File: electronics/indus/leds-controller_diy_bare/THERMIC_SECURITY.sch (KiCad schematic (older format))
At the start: 8 parts

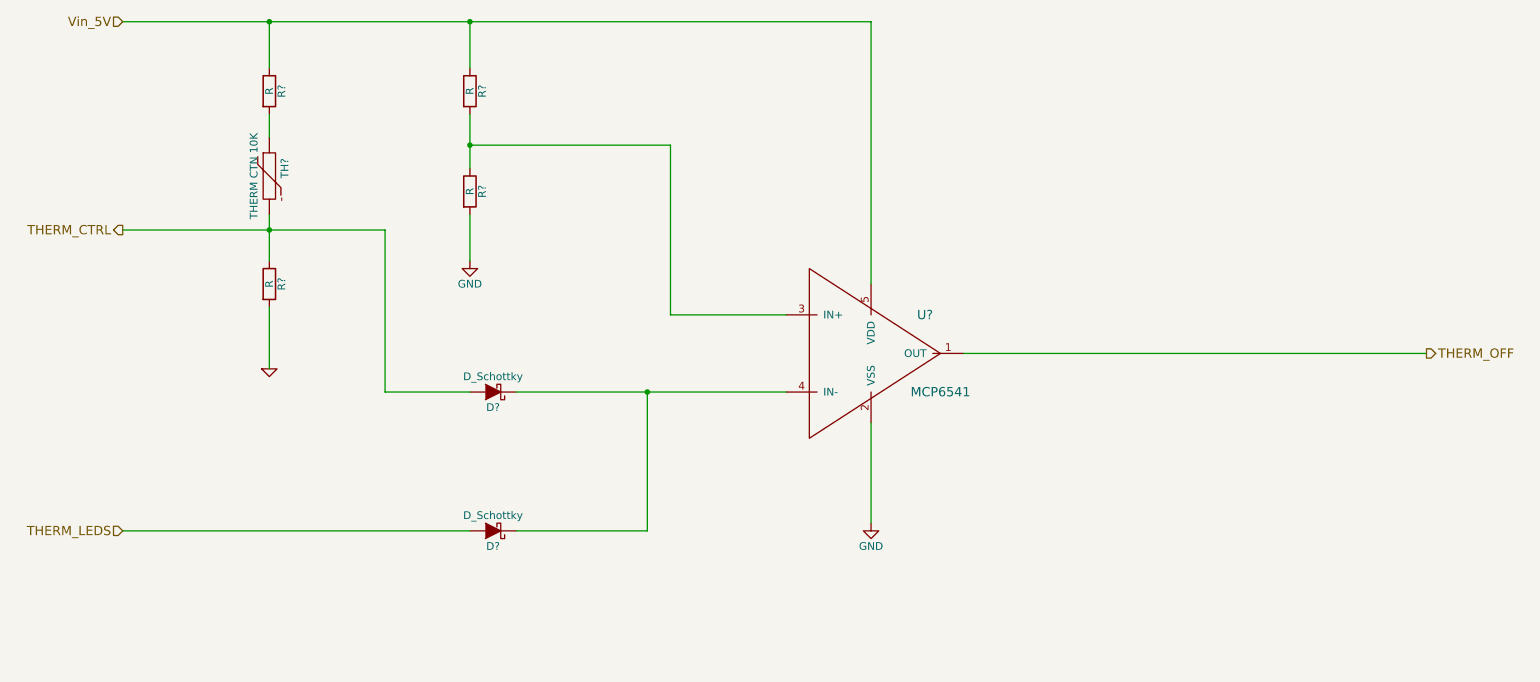
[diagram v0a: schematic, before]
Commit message: schema prctically ok missing refs
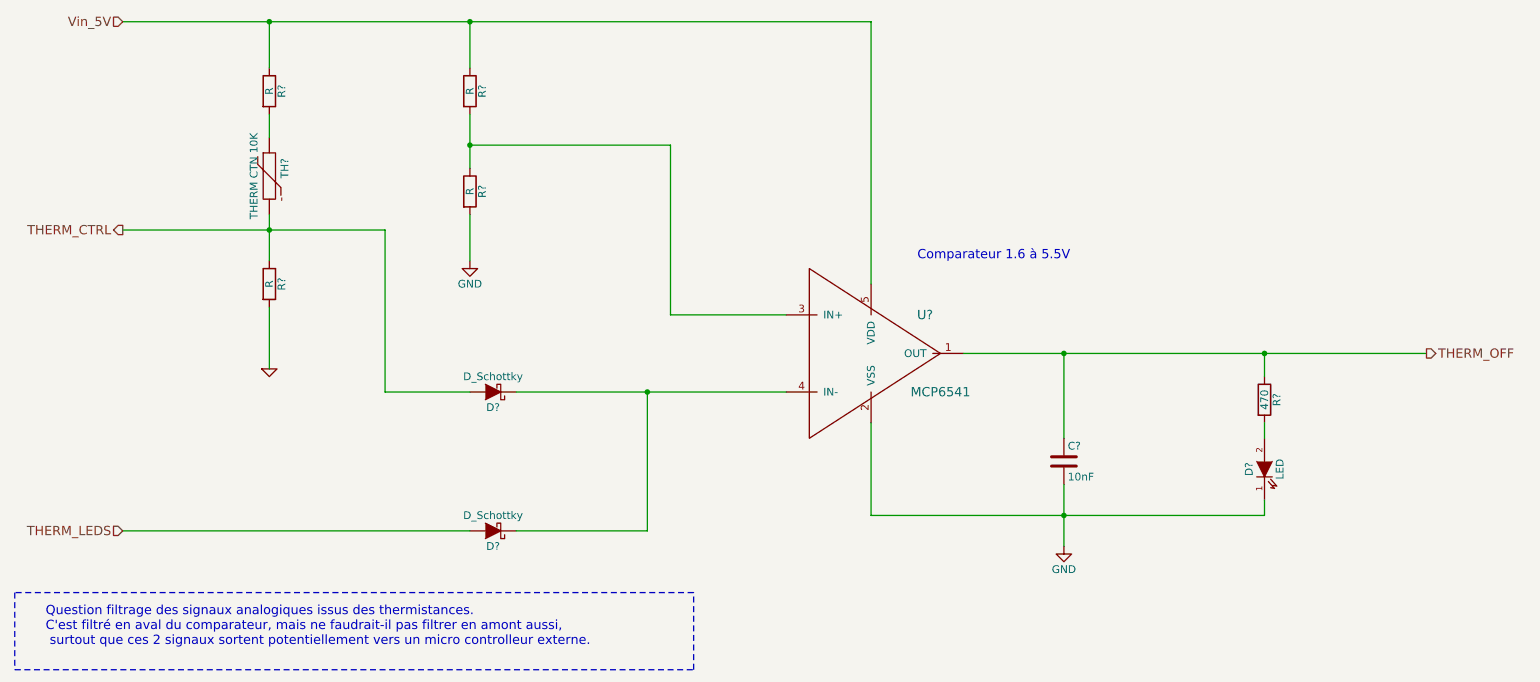
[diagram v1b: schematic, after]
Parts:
- added C?: 10nF, symbol C
- added D?: LED, symbol LED
- added R?: 470, symbol R
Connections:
- net GND: now also C?.2, D?.1 (K)
- net THERM_OFF: now also C?.1, R?.1
- new net: D?.2 (A), R?.2
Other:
- note added: "Comparateur 1.6 à 5.5V"
- note added: "Question filtrage des signaux analogiques issus des thermistances. \nC'est filtré en aval du comparateur, mais ne faudrait-il pas filtrer en amont aussi,\n surtout que ces 2 signaux sortent potentiellement vers un micro controlleur externe."
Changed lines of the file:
@@
 	1450 4950 3700 4950
 Wire Wire Line
-	1450 1650 2400 1650
-Wire Wire Line
-	2400 1650 3700 1650
-Wire Wire Line
-	3700 1650 6300 1650
+	1450 1650 6300 1650
 Wire Wire Line
 	6300 1650 6300 3350
-$Comp
-L GND #PWR?
-U 1 1 57638CC5
-P 6300 4900
-F 0 "#PWR?" H 6300 4650 50  0001 C CNN
-F 1 "GND" H 6300 4750 50  0000 C CNN
-F 2 "" H 6300 4900 50  0000 C CNN
-F 3 "" H 6300 4900 50  0000 C CNN
-	1    6300 4900
-	1    0    0    -1
-$EndComp
 Wire Wire Line
-	6300 4250 6300 4900
+	6300 4250 6300 4850
 $Comp
 L R R?
@@
 	3700 3200 3700 2900
 Wire Wire Line
-	3700 2250 3700 2450
-Wire Wire Line
-	3700 2450 3700 2600
+	3700 2250 3700 2600
 Wire Wire Line
 	3700 1950 3700 1650
@@
 $EndComp
 Wire Wire Line
-	2400 2900 2400 3000
+	2400 2900 2400 3200
 Wire Wire Line
-	2400 3000 2400 3200
-Wire Wire Line
-	1450 3000 2400 3000
-Wire Wire Line
-	2400 3000 3150 3000
+	1450 3000 3150 3000
 Wire Wire Line
 	3150 4050 3700 4050
 Wire Wire Line
-	4000 4050 4850 4050
-Wire Wire Line
-	4850 4050 5750 4050
+	4000 4050 5750 4050
 Wire Wire Line
 	4000 4950 4850 4950
@@
 Text HLabel 1450 3000 0    60   Output ~ 0
 THERM_CTRL
+$Comp
+L GND #PWR?
+U 1 1 5763C8DD
+P 7550 5050
+F 0 "#PWR?" H 7550 4800 50  0001 C CNN
+F 1 "GND" H 7550 4900 50  0000 C CNN
+F 2 "" H 7550 5050 50  0000 C CNN
+F 3 "" H 7550 5050 50  0000 C CNN
+	1    7550 5050
+	1    0    0    -1
+$EndComp
+$Comp
+L C C?
+U 1 1 5763C901
+P 7550 4500
+F 0 "C?" H 7575 4600 50  0000 L CNN
+F 1 "10nF" H 7575 4400 50  0000 L CNN
+F 2 "" H 7588 4350 50  0000 C CNN
+F 3 "" H 7550 4500 50  0000 C CNN
+	1    7550 4500
+	1    0    0    -1
+$EndComp
+Wire Wire Line
+	7550 4350 7550 3800
+Connection ~ 7550 3800
+Wire Wire Line
+	7550 4650 7550 5050
+$Comp
+L LED D?
+U 1 1 576465EC
+P 8850 4550
+F 0 "D?" H 8850 4650 50  0000 C CNN
+F 1 "LED" H 8850 4450 50  0000 C CNN
+F 2 "" H 8850 4550 50  0000 C CNN
+F 3 "" H 8850 4550 50  0000 C CNN
+	1    8850 4550
+	0    -1   -1   0
+$EndComp
+Connection ~ 8850 3800
+Wire Wire Line
+	6300 4850 8850 4850
+Connection ~ 7550 4850
+$Comp
+L R R?
+U 1 1 5764C339
+P 8850 4100
+F 0 "R?" V 8930 4100 50  0000 C CNN
+F 1 "470" V 8850 4100 50  0000 C CNN
+F 2 "" V 8780 4100 50  0000 C CNN
+F 3 "" H 8850 4100 50  0000 C CNN
+	1    8850 4100
+	1    0    0    -1
+$EndComp
+Wire Wire Line
+	8850 3800 8850 3950
+Wire Wire Line
+	8850 4250 8850 4350
+Wire Wire Line
+	8850 4850 8850 4750
+Text Notes 950  5700 0    60   ~ 0
+Question filtrage des signaux analogiques issus des thermistances. \nC'est filtré en aval du comparateur, mais ne faudrait-il pas filtrer en amont aussi,\n surtout que ces 2 signaux sortent potentiellement vers un micro controlleur externe.
+Wire Notes Line
+	750  5850 5150 5850
+Wire Notes Line
+	5150 5850 5150 5350
+Wire Notes Line
+	5150 5350 750  5350
+Wire Notes Line
+	750  5350 750  5850
+Text Notes 6600 3200 0    60   ~ 0
+Comparateur 1.6 à 5.5V
 $EndSCHEMATC

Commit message: schema prctically ok missing refs
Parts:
- gave numbers to parts that had none: 11
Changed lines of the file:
@@
 THERM_OFF
 $Comp
-L THERMISTOR TH?
+L THERMISTOR TH1
 U 1 1 57630E89
 P 2400 2650
-F 0 "TH?" V 2500 2700 50  0000 C CNN
+F 0 "TH1" V 2500 2700 50  0000 C CNN
 F 1 "THERM CTN 10K" V 2300 2650 50  0000 C CNN
 F 2 "" H 2400 2650 60  0000 C CNN
@@
 $EndComp
 $Comp
-L GND-RESCUE-leds-controller #PWR?
+L GND-RESCUE-leds-controller #PWR19
 U 1 1 57630E97
 P 2400 3900
-F 0 "#PWR?" H 2400 3900 30  0001 C CNN
+F 0 "#PWR19" H 2400 3900 30  0001 C CNN
 F 1 "GND" H 2400 3830 30  0001 C CNN
 F 2 "" H 2400 3900 60  0000 C CNN
@@
 Vin_5V
 $Comp
-L D_Schottky D?
+L D_Schottky D11
 U 1 1 57637B98
 P 3850 4950
-F 0 "D?" H 3850 5050 50  0000 C CNN
+F 0 "D11" H 3850 5050 50  0000 C CNN
 F 1 "D_Schottky" H 3850 4850 50  0000 C CNN
 F 2 "" H 3850 4950 50  0000 C CNN
@@
 $EndComp
 $Comp
-L D_Schottky D?
+L D_Schottky D10
 U 1 1 576385E9
 P 3850 4050
-F 0 "D?" H 3850 4150 50  0000 C CNN
+F 0 "D10" H 3850 4150 50  0000 C CNN
 F 1 "D_Schottky" H 3850 3950 50  0000 C CNN
 F 2 "" H 3850 4050 50  0000 C CNN
@@
 $EndComp
 $Comp
-L MCP6541 U?
+L MCP6541 U7
 U 1 1 57638931
 P 6250 3800
-F 0 "U?" H 6650 4050 60  0000 C CNN
+F 0 "U7" H 6650 4050 60  0000 C CNN
 F 1 "MCP6541" H 6750 3550 60  0000 C CNN
 F 2 "" H 6300 3800 60  0000 C CNN
@@
 	6300 4250 6300 4850
 $Comp
-L R R?
+L R R43
 U 1 1 57638D88
 P 3700 2100
-F 0 "R?" V 3780 2100 50  0000 C CNN
+F 0 "R43" V 3780 2100 50  0000 C CNN
 F 1 "R" V 3700 2100 50  0000 C CNN
 F 2 "" V 3630 2100 50  0000 C CNN
@@
 $EndComp
 $Comp
-L R R?
+L R R44
 U 1 1 57638DE9
 P 3700 2750
-F 0 "R?" V 3780 2750 50  0000 C CNN
+F 0 "R44" V 3780 2750 50  0000 C CNN
 F 1 "R" V 3700 2750 50  0000 C CNN
 F 2 "" V 3630 2750 50  0000 C CNN
@@
 $EndComp
 $Comp
-L GND #PWR?
+L GND #PWR20
 U 1 1 57638E5C
 P 3700 3200
-F 0 "#PWR?" H 3700 2950 50  0001 C CNN
+F 0 "#PWR20" H 3700 2950 50  0001 C CNN
 F 1 "GND" H 3700 3050 50  0000 C CNN
 F 2 "" H 3700 3200 50  0000 C CNN
@@
 Connection ~ 3700 2450
 $Comp
-L R R?
+L R R31
 U 1 1 57638FD4
 P 2400 2100
-F 0 "R?" V 2480 2100 50  0000 C CNN
+F 0 "R31" V 2480 2100 50  0000 C CNN
 F 1 "R" V 2400 2100 50  0000 C CNN
 F 2 "" V 2330 2100 50  0000 C CNN
@@
 Connection ~ 2400 1650
 $Comp
-L R R?
+L R R42
 U 1 1 57639066
 P 2400 3350
-F 0 "R?" V 2480 3350 50  0000 C CNN
+F 0 "R42" V 2480 3350 50  0000 C CNN
 F 1 "R" V 2400 3350 50  0000 C CNN
 F 2 "" V 2330 3350 50  0000 C CNN
@@
 THERM_CTRL
 $Comp
-L GND #PWR?
+L GND #PWR21
 U 1 1 5763C8DD
 P 7550 5050
-F 0 "#PWR?" H 7550 4800 50  0001 C CNN
+F 0 "#PWR21" H 7550 4800 50  0001 C CNN
 F 1 "GND" H 7550 4900 50  0000 C CNN
 F 2 "" H 7550 5050 50  0000 C CNN
@@
 $EndComp
 $Comp
-L C C?
+L C C20
 U 1 1 5763C901
 P 7550 4500
-F 0 "C?" H 7575 4600 50  0000 L CNN
+F 0 "C20" H 7575 4600 50  0000 L CNN
 F 1 "10nF" H 7575 4400 50  0000 L CNN
 F 2 "" H 7588 4350 50  0000 C CNN
@@
 	7550 4650 7550 5050
 $Comp
-L LED D?
+L LED D12
 U 1 1 576465EC
 P 8850 4550
-F 0 "D?" H 8850 4650 50  0000 C CNN
+F 0 "D12" H 8850 4650 50  0000 C CNN
 F 1 "LED" H 8850 4450 50  0000 C CNN
 F 2 "" H 8850 4550 50  0000 C CNN
@@
 Connection ~ 7550 4850
 $Comp
-L R R?
+L R R45
 U 1 1 5764C339
 P 8850 4100
-F 0 "R?" V 8930 4100 50  0000 C CNN
+F 0 "R45" V 8930 4100 50  0000 C CNN
 F 1 "470" V 8850 4100 50  0000 C CNN
 F 2 "" V 8780 4100 50  0000 C CNN

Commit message: bom refs etc
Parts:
- removed R31: R, symbol R
- D10, D11: value D_Schottky -> DB2J31300L
- D12: value LED -> KP-3216SRC-PRV
- R42: value R -> 2.55K
- R43: value R -> 600
- R44: value R -> 2.5K
- TH1: value THERM CTN 10K -> NTCS0805E3103JMT
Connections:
- net Vin_5V: now also TH1.1
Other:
- note added: "1V à 25°, 4V à 115°"
- note added: "4V : le seuil pour couper les controlleurs"
- moved on the sheet: TH1
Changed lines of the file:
@@
 L THERMISTOR TH1
 U 1 1 57630E89
-P 2400 2650
-F 0 "TH1" V 2500 2700 50  0000 C CNN
-F 1 "THERM CTN 10K" V 2300 2650 50  0000 C CNN
-F 2 "" H 2400 2650 60  0000 C CNN
-F 3 "" H 2400 2650 60  0000 C CNN
-	1    2400 2650
+P 2400 2350
+F 0 "TH1" V 2500 2400 50  0000 C CNN
+F 1 "NTCS0805E3103JMT" V 2300 2350 50  0000 C CNN
+F 2 "" H 2400 2350 60  0000 C CNN
+F 3 "" H 2400 2350 60  0000 C CNN
+	1    2400 2350
 	1    0    0    -1
 $EndComp
@@
 P 3850 4950
 F 0 "D11" H 3850 5050 50  0000 C CNN
-F 1 "D_Schottky" H 3850 4850 50  0000 C CNN
+F 1 "DB2J31300L" H 3850 4850 50  0000 C CNN
 F 2 "" H 3850 4950 50  0000 C CNN
 F 3 "" H 3850 4950 50  0000 C CNN
@@
 P 3850 4050
 F 0 "D10" H 3850 4150 50  0000 C CNN
-F 1 "D_Schottky" H 3850 3950 50  0000 C CNN
+F 1 "DB2J31300L" H 3850 3950 50  0000 C CNN
 F 2 "" H 3850 4050 50  0000 C CNN
 F 3 "" H 3850 4050 50  0000 C CNN
@@
 	1450 4950 3700 4950
 Wire Wire Line
-	1450 1650 6300 1650
+	1450 1650 2400 1650
+Wire Wire Line
+	2400 1650 3700 1650
+Wire Wire Line
+	3700 1650 6300 1650
 Wire Wire Line
 	6300 1650 6300 3350
@@
 P 3700 2100
 F 0 "R43" V 3780 2100 50  0000 C CNN
-F 1 "R" V 3700 2100 50  0000 C CNN
+F 1 "600" V 3700 2100 50  0000 C CNN
 F 2 "" V 3630 2100 50  0000 C CNN
 F 3 "" H 3700 2100 50  0000 C CNN
@@
 P 3700 2750
 F 0 "R44" V 3780 2750 50  0000 C CNN
-F 1 "R" V 3700 2750 50  0000 C CNN
+F 1 "2.5K" V 3700 2750 50  0000 C CNN
 F 2 "" V 3630 2750 50  0000 C CNN
 F 3 "" H 3700 2750 50  0000 C CNN
@@
 	3700 3200 3700 2900
 Wire Wire Line
-	3700 2250 3700 2600
+	3700 2250 3700 2450
+Wire Wire Line
+	3700 2450 3700 2600
 Wire Wire Line
 	3700 1950 3700 1650
@@
 	5000 3550 5750 3550
 Connection ~ 3700 2450
-$Comp
-L R R31
-U 1 1 57638FD4
-P 2400 2100
-F 0 "R31" V 2480 2100 50  0000 C CNN
-F 1 "R" V 2400 2100 50  0000 C CNN
-F 2 "" V 2330 2100 50  0000 C CNN
-F 3 "" H 2400 2100 50  0000 C CNN
-	1    2400 2100
-	1    0    0    -1
-$EndComp
-Wire Wire Line
-	2400 1950 2400 1650
+Wire Wire Line
+	2400 1650 2400 2100
 Connection ~ 2400 1650
 $Comp
@@
 P 2400 3350
 F 0 "R42" V 2480 3350 50  0000 C CNN
-F 1 "R" V 2400 3350 50  0000 C CNN
+F 1 "2.55K" V 2400 3350 50  0000 C CNN
 F 2 "" V 2330 3350 50  0000 C CNN
 F 3 "" H 2400 3350 50  0000 C CNN
@@
 $EndComp
 Wire Wire Line
-	2400 2900 2400 3200
-Wire Wire Line
-	1450 3000 3150 3000
+	2400 2600 2400 3000
+Wire Wire Line
+	2400 3000 2400 3200
+Wire Wire Line
+	1450 3000 2400 3000
+Wire Wire Line
+	2400 3000 3150 3000
 Wire Wire Line
 	3150 4050 3700 4050
 Wire Wire Line
-	4000 4050 5750 4050
+	4000 4050 4850 4050
+Wire Wire Line
+	4850 4050 5750 4050
 Wire Wire Line
 	4000 4950 4850 4950
@@
 Connection ~ 4850 4050
 Wire Wire Line
-	6900 3800 9900 3800
+	6900 3800 7550 3800
+Wire Wire Line
+	7550 3800 8850 3800
+Wire Wire Line
+	8850 3800 9900 3800
 Connection ~ 2400 3000
 Wire Wire Line
 	3150 3000 3150 4050
-Wire Wire Line
-	2400 2400 2400 2250
 Text HLabel 1450 3000 0    60   Output ~ 0
 THERM_CTRL
@@
 Connection ~ 7550 3800
 Wire Wire Line
-	7550 4650 7550 5050
+	7550 4650 7550 4850
+Wire Wire Line
+	7550 4850 7550 5050
 $Comp
 L LED D12
@@
 P 8850 4550
 F 0 "D12" H 8850 4650 50  0000 C CNN
-F 1 "LED" H 8850 4450 50  0000 C CNN
+F 1 "KP-3216SRC-PRV" H 8750 4400 50  0000 C CNN
 F 2 "" H 8850 4550 50  0000 C CNN
 F 3 "" H 8850 4550 50  0000 C CNN
@@
 Connection ~ 8850 3800
 Wire Wire Line
-	6300 4850 8850 4850
+	6300 4850 7550 4850
+Wire Wire Line
+	7550 4850 8850 4850
 Connection ~ 7550 4850
 $Comp
@@
 Text Notes 6600 3200 0    60   ~ 0
 Comparateur 1.6 à 5.5V
+Text Notes 2500 2950 0    60   ~ 0
+1V à 25°, 4V à 115°
+Text Notes 3750 2400 0    60   ~ 0
+4V : le seuil pour couper les controlleurs
 $EndSCHEMATC

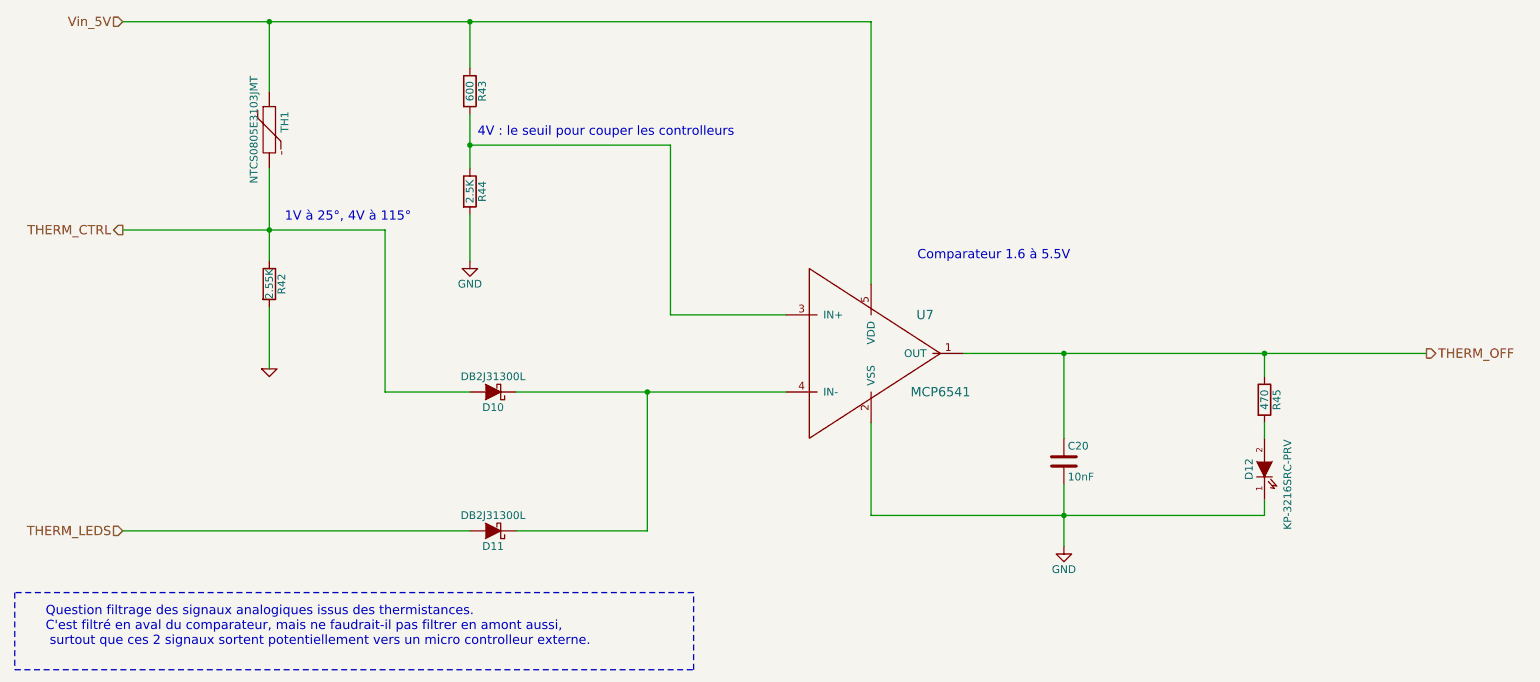
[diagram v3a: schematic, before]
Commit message: simpler schematics with a lot of values now
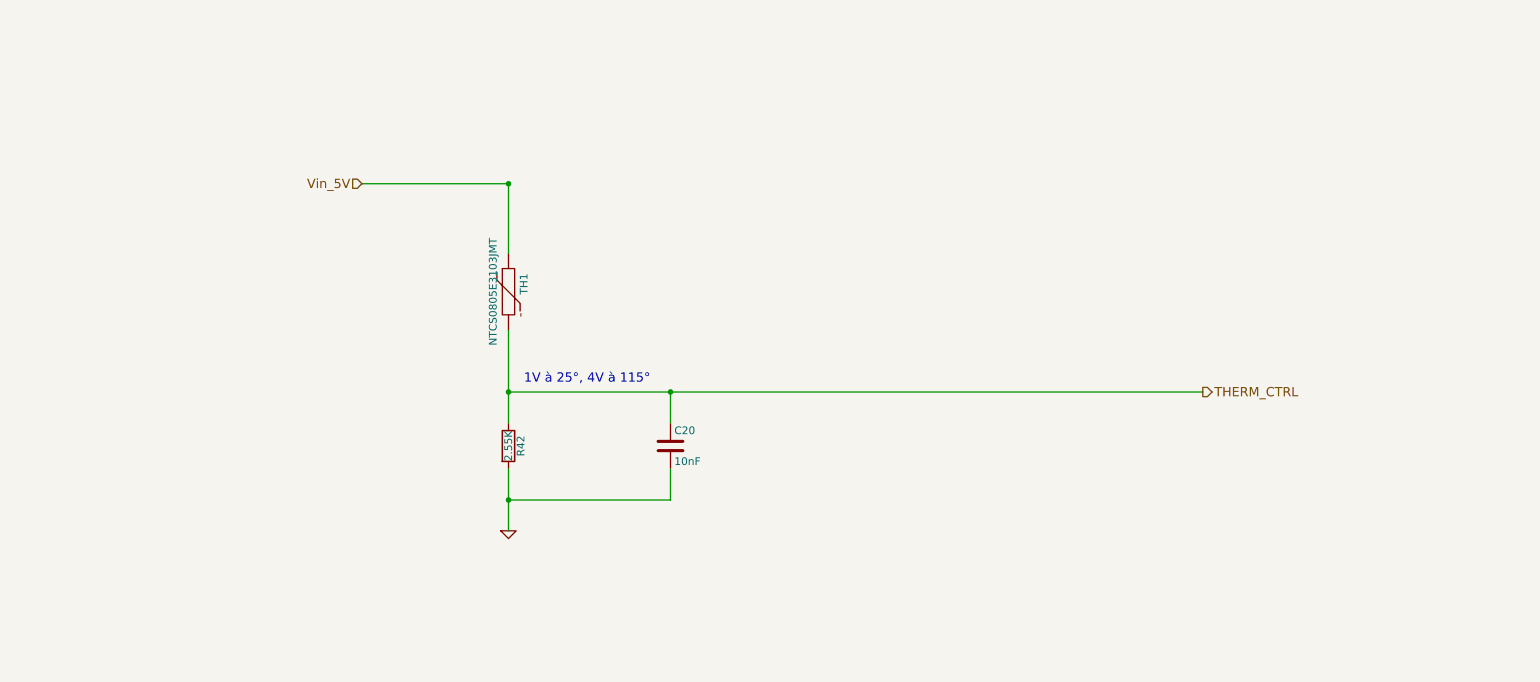
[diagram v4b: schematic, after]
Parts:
- removed D10, D11: DB2J31300L, symbol D_Schottky
- removed D12: KP-3216SRC-PRV, symbol LED
- removed R43: 600, symbol R
- removed R44: 2.5K, symbol R
- removed R45: 470, symbol R
- removed U7: MCP6541, symbol MCP6541
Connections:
- net THERM_OFF is gone; now on net THERM_CTRL: C20.1
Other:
- note removed: "4V : le seuil pour couper les controlleurs"
- note removed: "Comparateur 1.6 à 5.5V"
- note removed: "Question filtrage des signaux analogiques issus des thermistances. \nC'est filtré en aval du comparateur, mais ne faudrait-il pas filtrer en amont aussi,\n surtout que ces 2 signaux sortent potentiellement vers un micro controlleur externe."
- moved on the sheet: C20, R42, TH1

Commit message: footprint with libraries
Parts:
- C20: footprint (none) -> Capacitors_SMD:C_1206
- R42: footprint (none) -> Resistors_SMD:R_0805
- TH1: footprint (none) -> risebox:THERM_NTCS0603E3272JMT_SMD0603
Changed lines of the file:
@@
 F 0 "TH1" V 4050 3450 50  0000 C CNN
 F 1 "NTCS0805E3103JMT" V 3850 3400 50  0000 C CNN
-F 2 "" H 3950 3400 60  0000 C CNN
+F 2 "risebox:THERM_NTCS0603E3272JMT_SMD0603" H 3950 3400 60  0001 C CNN
 F 3 "" H 3950 3400 60  0000 C CNN
 	1    3950 3400
@@
 $EndComp
 $Comp
-L GND-RESCUE-leds-controller #PWR19
+L GND-RESCUE-leds-controller #PWR020
 U 1 1 57630E97
 P 3950 4950
-F 0 "#PWR19" H 3950 4950 30  0001 C CNN
+F 0 "#PWR020" H 3950 4950 30  0001 C CNN
 F 1 "GND" H 3950 4880 30  0001 C CNN
 F 2 "" H 3950 4950 60  0000 C CNN
@@
 F 0 "R42" V 4030 4400 50  0000 C CNN
 F 1 "2.55K" V 3950 4400 50  0000 C CNN
-F 2 "" V 3880 4400 50  0000 C CNN
+F 2 "Resistors_SMD:R_0805" V 3880 4400 50  0001 C CNN
 F 3 "" H 3950 4400 50  0000 C CNN
 	1    3950 4400
@@
 F 0 "C20" H 5025 4500 50  0000 L CNN
 F 1 "10nF" H 5025 4300 50  0000 L CNN
-F 2 "" H 5038 4250 50  0000 C CNN
+F 2 "Capacitors_SMD:C_1206" H 5038 4250 50  0001 C CNN
 F 3 "" H 5000 4400 50  0000 C CNN
 	1    5000 4400
